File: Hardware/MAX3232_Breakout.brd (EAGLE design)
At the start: 25.4 x 14 mm, 12 parts, among them U1 MAX3232

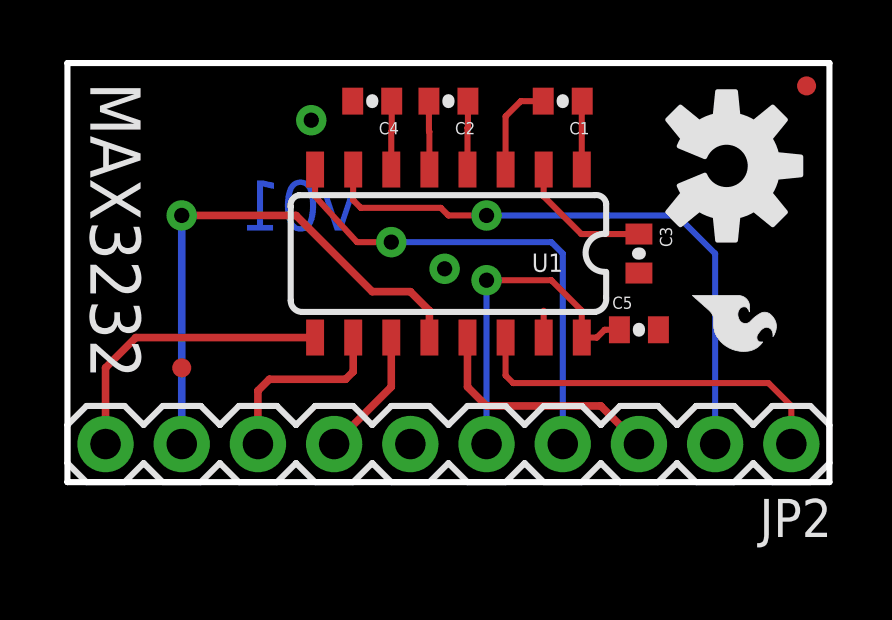
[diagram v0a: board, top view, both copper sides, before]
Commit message: Updated to 0603, added attributes.
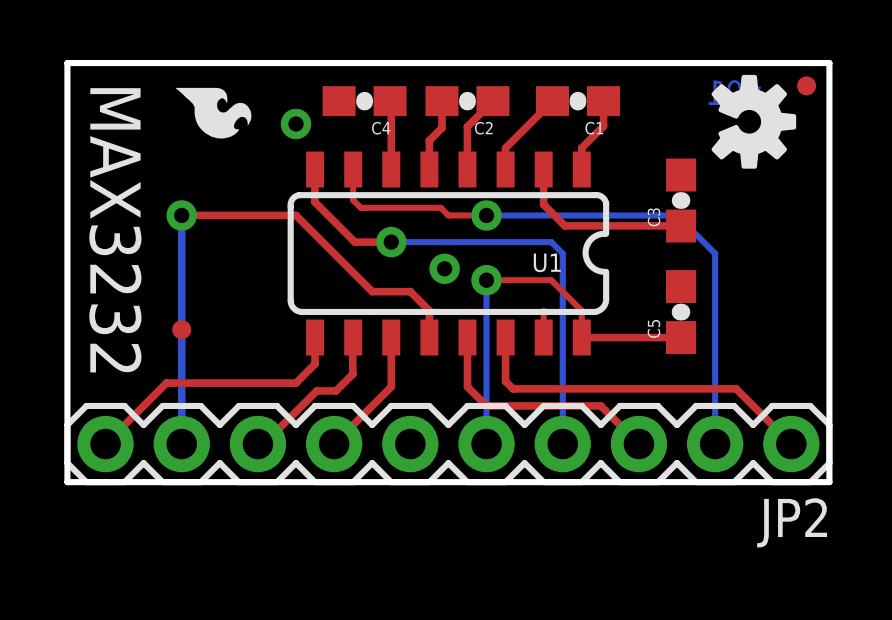
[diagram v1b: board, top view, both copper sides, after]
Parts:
- removed JP1: LOGO-SFESK, SparkFun-Aesthetics:SFE-LOGO-FLAME
- added LOGO1: SFE_LOGO_FLAME.1_INCH, SparkFun-Aesthetics:SFE_LOGO_FLAME_.1
- C1, C2, C3, C4, C5: device SparkFun-Passives:0402-CAP -> SparkFun-Capacitors:0603-CAP
- U$1: value OSHW-LOGOM -> OSHW-LOGOS; device SparkFun-Aesthetics:OSHW-LOGO-M -> SparkFun-Aesthetics:OSHW-LOGO-S
- moved C3 2.26 mm to (20.5, 9.39), turned to 90 degrees
- moved U$1 1.65 mm to (22.7, 12.0)
- moved C5 1.52 mm to (20.5, 5.67), turned to 90 degrees
- moved JP4 1.27 mm to (3.81, 5.08)
- moved C2 0.64 mm to (13.3, 12.7)
- moved C1 0.51 mm to (17.0, 12.7)
- moved C4 0.25 mm to (9.91, 12.7)
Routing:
- net VCC: track 11.3 -> 13.3 mm
- net V+: track 4.59 -> 6.04 mm
- net T2IN: track 6.35 -> 5.35 mm
- net R2OUT: track 9.94 -> 8.97 mm
- net T1OUT: track 12.5 -> 11.9 mm

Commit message: Fixed SCH, re route trace and trestrict
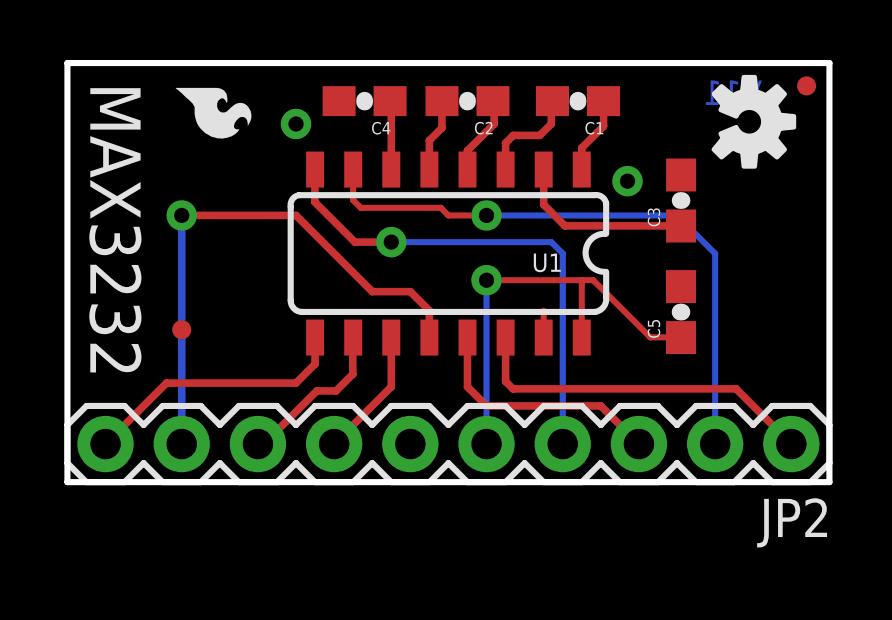
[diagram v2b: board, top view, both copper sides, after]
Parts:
- FRAME1: value FRAME-LETTER -> (none)
- moved FRAME1 53.9 mm to (-12.7, -14.0)
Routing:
- net VCC: track 13.3 -> 14.6 mm
- net C1-: track 2.93 -> 3.45 mm
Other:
- board text added: "M Hord"
- board text added: "Revised by:Patrick Alberts"
- board text added: "V11"
- board text removed: "v01"
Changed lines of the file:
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@@
 <text x="10.541" y="2.54" size="1.6764" layer="22" font="vector" ratio="15" rot="MR90">GND</text>
 <text x="13.081" y="2.54" size="1.6764" layer="22" font="vector" ratio="15" rot="MR90">3V-5.5V</text>
-<text x="23.1521" y="12.573" size="0.8128" layer="16" font="vector" ratio="15" rot="MR0">v01</text>
+<text x="23.1521" y="12.573" size="0.8128" layer="16" font="vector" ratio="15" rot="MR0">V11</text>
 <text x="-38.1" y="0" size="1.6764" layer="27" ratio="15">Mike Hord</text>
 <dimension x1="-5.08" y1="0" x2="-5.08" y2="13.97" x3="-6.35" y3="6.985" textsize="1.778" textratio="15" layer="47"/>
 <dimension x1="0" y1="19.05" x2="25.4" y2="19.05" x3="12.7" y3="20.32" textsize="1.778" textratio="15" layer="47"/>
+<text x="-1.143" y="-16.891" size="1.778" layer="51" font="vector" ratio="10">Revised by:Patrick Alberts</text>
+<text x="13.335" y="-13.97" size="1.778" layer="51" font="vector" ratio="10">M Hord</text>
+<rectangle x1="17.145" y1="7.239" x2="17.78" y2="7.62" layer="41"/>
+<rectangle x1="7.493" y1="5.715" x2="8.89" y2="7.366" layer="41"/>
 </plain>
 <attributes>
@@
 <attribute name="NO_PART" value="1" x="22.727921875" y="12.011659375" size="1.778" layer="27" rot="R270" display="off"/>
 </element>
-<element name="FRAME1" library="SparkFun-Aesthetics" package="CREATIVE_COMMONS" value="FRAME-LETTER" x="-64.7684125" y="0">
-<attribute name="NO_PART" value="1" x="-64.7684125" y="0" size="1.778" layer="27" display="off"/>
+<element name="FRAME1" library="SparkFun-Aesthetics" package="CREATIVE_COMMONS" value="" x="-12.6984125" y="-13.97" smashed="yes">
+<attribute name="NO_PART" value="1" x="-12.6984125" y="-13.97" size="1.778" layer="27" display="off"/>
+<attribute name="VERSION" value="v01" x="16.5115875" y="-3.81" size="1.27" layer="16" font="vector" ratio="15" rot="SMR0" display="off"/>
+<attribute name="DESIGNER" value="NAME" x="13.9715875" y="-13.97" size="1.778" layer="51" display="off"/>
 </element>
 <element name="C5" library="SparkFun-Capacitors" package="0603-CAP" value=".1uF" x="20.45208125" y="5.669278125" smashed="yes" rot="R90">
@@
 <contactref element="U1" pad="4"/>
 <wire x1="13.332459375" y1="10.422540625" x2="13.335" y2="10.42" width="0.254" layer="1"/>
-<wire x1="13.332459375" y1="10.422540625" x2="13.332459375" y2="11.847459375" width="0.254" layer="1"/>
-<wire x1="13.332459375" y1="11.847459375" x2="14.185" y2="12.7" width="0.254" layer="1"/>
+<wire x1="13.332459375" y1="10.422540625" x2="13.332459375" y2="11.046459375" width="0.254" layer="1"/>
+<wire x1="13.332459375" y1="11.046459375" x2="14.224" y2="11.938" width="0.254" layer="1"/>
+<wire x1="14.224" y1="11.938" x2="14.224" y2="12.661" width="0.254" layer="1"/>
+<wire x1="14.224" y1="12.661" x2="14.185" y2="12.7" width="0.254" layer="1"/>
 </signal>
 <signal name="C1-">
 <contactref element="U1" pad="3"/>
 <contactref element="C1" pad="2"/>
-<wire x1="14.605" y1="10.42" x2="14.605" y2="11.137" width="0.254" layer="1"/>
-<wire x1="14.605" y1="11.137" x2="16.168" y2="12.7" width="0.254" layer="1"/>
+<wire x1="14.605" y1="10.42" x2="14.605" y2="11.303" width="0.254" layer="1"/>
+<wire x1="14.605" y1="11.303" x2="14.859" y2="11.557" width="0.254" layer="1"/>
+<wire x1="14.859" y1="11.557" x2="15.748" y2="11.557" width="0.254" layer="1"/>
+<wire x1="15.748" y1="11.557" x2="16.129" y2="11.938" width="0.254" layer="1"/>
+<wire x1="16.129" y1="11.938" x2="16.129" y2="12.661" width="0.254" layer="1"/>
+<wire x1="16.129" y1="12.661" x2="16.168" y2="12.7" width="0.254" layer="1"/>
 </signal>
 <signal name="C1+">
@@
 <wire x1="13.97" y1="6.731" x2="13.97" y2="1.27" width="0.2032" layer="16"/>
 <via x="13.97" y="6.731" extent="1-16" drill="0.508"/>
-<wire x1="17.145" y1="4.82" x2="17.145" y2="5.715" width="0.2032" layer="1"/>
-<wire x1="17.145" y1="5.715" x2="16.129" y2="6.731" width="0.2032" layer="1"/>
-<wire x1="13.97" y1="6.731" x2="16.129" y2="6.731" width="0.2032" layer="1"/>
+<wire x1="13.97" y1="6.731" x2="17.145" y2="6.731" width="0.2032" layer="1"/>
 <contactref element="C5" pad="1"/>
-<wire x1="17.145" y1="4.82" x2="20.451359375" y2="4.82" width="0.254" layer="1"/>
+<wire x1="17.145" y1="6.731" x2="17.526" y2="6.731" width="0.2032" layer="1"/>
 <wire x1="20.451359375" y1="4.82" x2="20.45208125" y2="4.819278125" width="0.254" layer="1"/>
+<wire x1="17.526" y1="6.731" x2="19.431" y2="4.826" width="0.2032" layer="1"/>
+<wire x1="19.431" y1="4.826" x2="20.445359375" y2="4.826" width="0.2032" layer="1"/>
+<wire x1="20.445359375" y1="4.826" x2="20.45208125" y2="4.819278125" width="0.2032" layer="1"/>
+<wire x1="17.145" y1="4.82" x2="17.145" y2="6.731" width="0.2032" layer="1"/>
 </signal>
 <signal name="V+">
@@
 </polygon>
 <wire x1="15.875" y1="4.82" x2="15.875" y2="5.715" width="0.2032" layer="1"/>
-<via x="12.573" y="7.112" extent="1-16" drill="0.508"/>
+<via x="18.669" y="10.033" extent="1-16" drill="0.508"/>
 <via x="7.62" y="11.938" extent="1-16" drill="0.508"/>
 <contactref element="C5" pad="2"/>
